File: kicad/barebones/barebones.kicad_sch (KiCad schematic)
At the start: 8 parts, among them J104 PAL-1 Expansion Connector, SW101 PICO RESET, SW103 SW_DIP_x02, U102 74LS145, U104 Pico

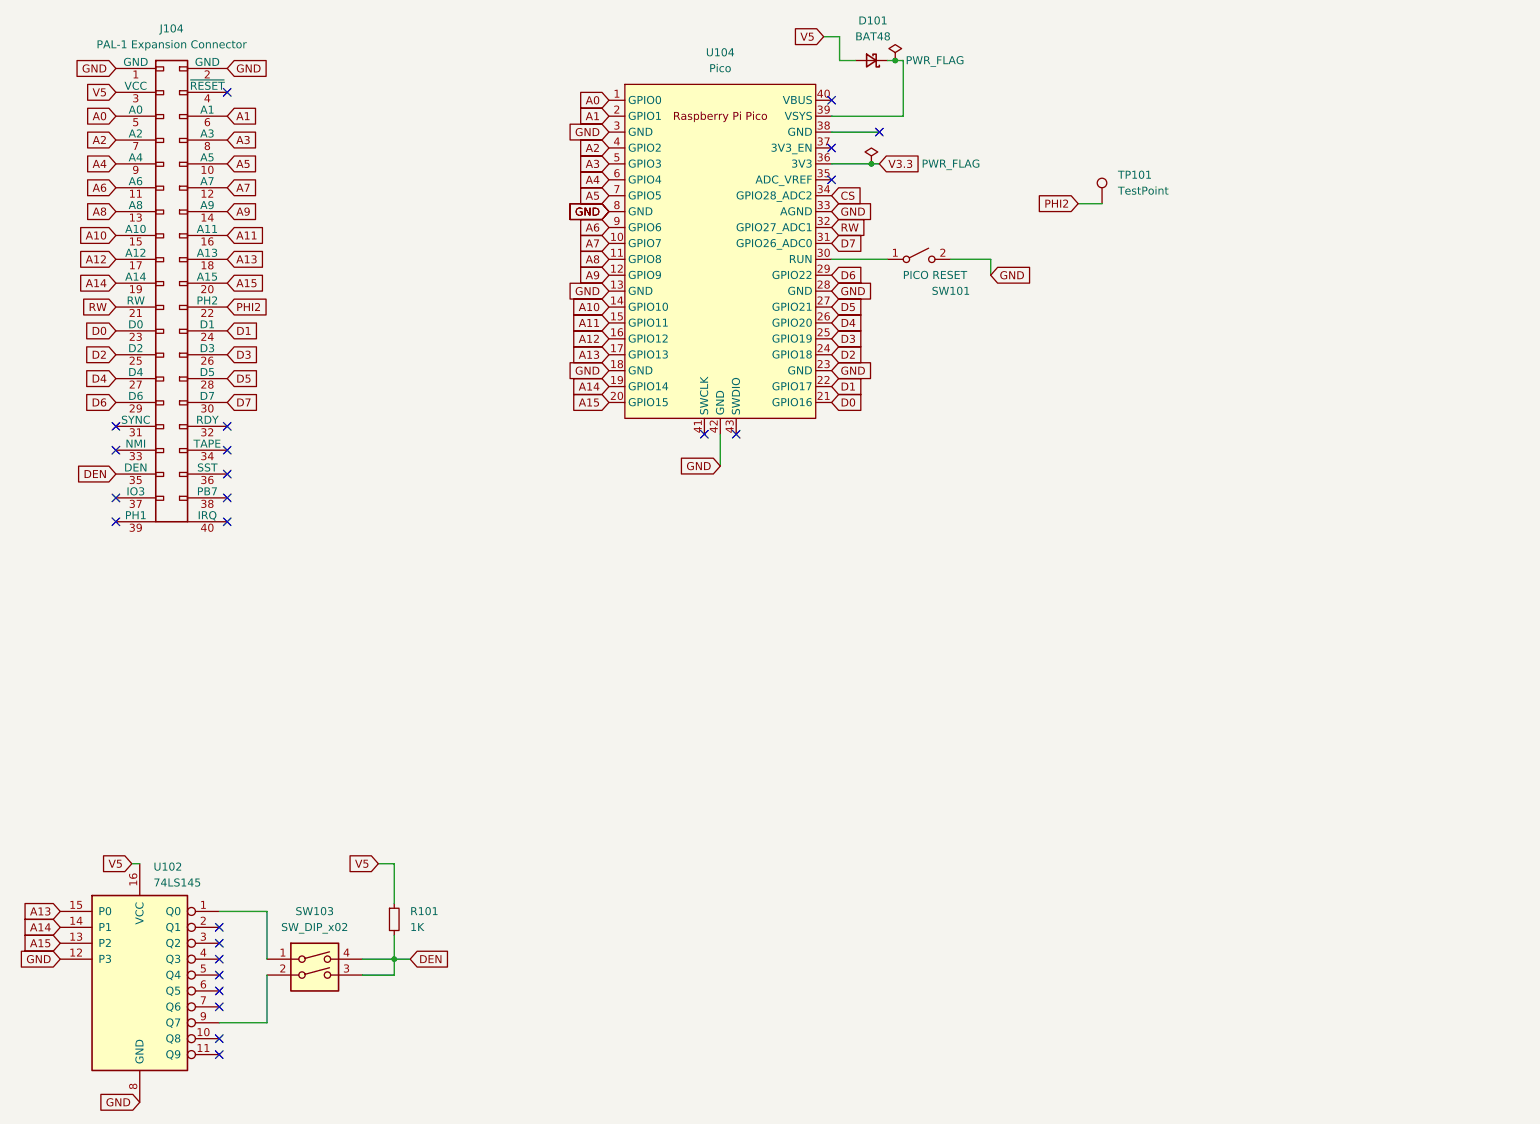
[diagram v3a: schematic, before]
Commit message: New PCB that is 100% software defined
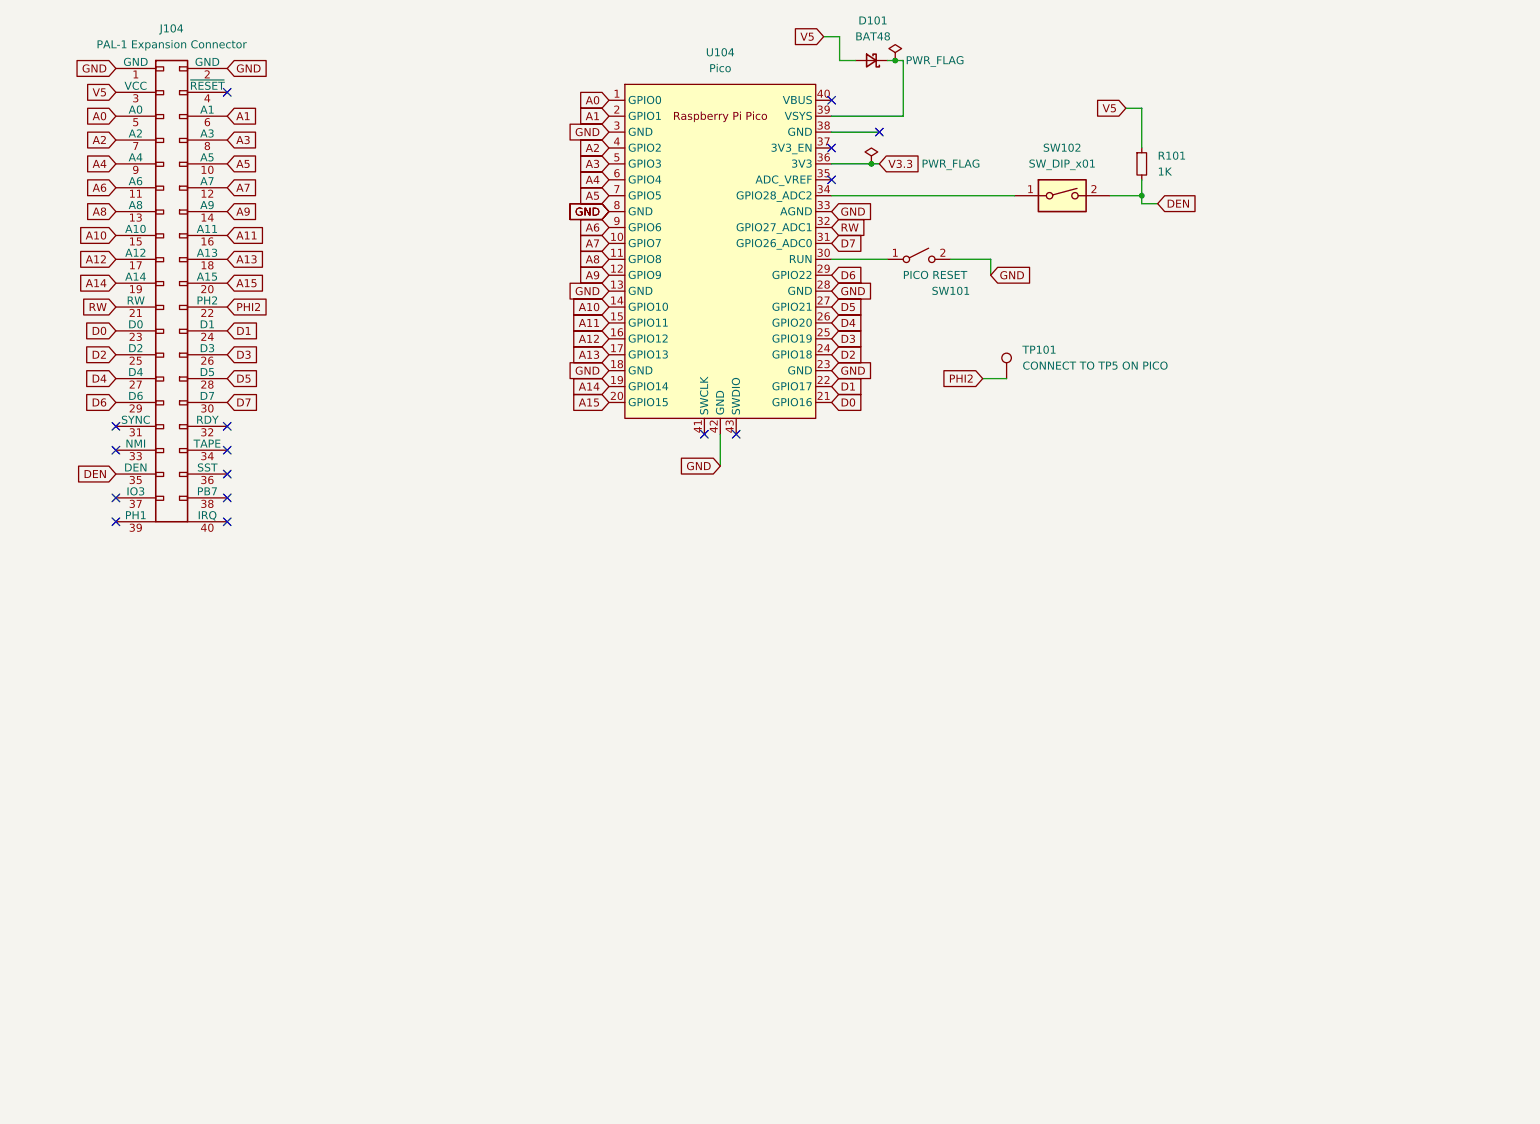
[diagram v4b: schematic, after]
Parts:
- removed SW103: SW_DIP_x02, Button_Switch_THT:SW_DIP_SPSTx02_Slide_9.78x7.26mm_W7.62mm_P2.54mm, symbol Switch:SW_DIP_x02
- removed U102: 74LS145, Package_DIP:DIP-16_W7.62mm_Socket_LongPads, symbol 74xx:74LS145
- added SW102: SW_DIP_x01, Button_Switch_THT:SW_DIP_SPSTx01_Slide_9.78x4.72mm_W7.62mm_P2.54mm, symbol Switch:SW_DIP_x01
- TP101: value TestPoint -> CONNECT TO TP5 ON PICO
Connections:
- net DEN: now also SW102.2
- net CS: no longer names the net of U104.34 (GPIO28_ADC2)
- net CS: now also SW102.1
- no-connect marks 24 -> 16
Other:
- moved on the sheet: R101, TP101
